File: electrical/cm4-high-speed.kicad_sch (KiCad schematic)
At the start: 1 part

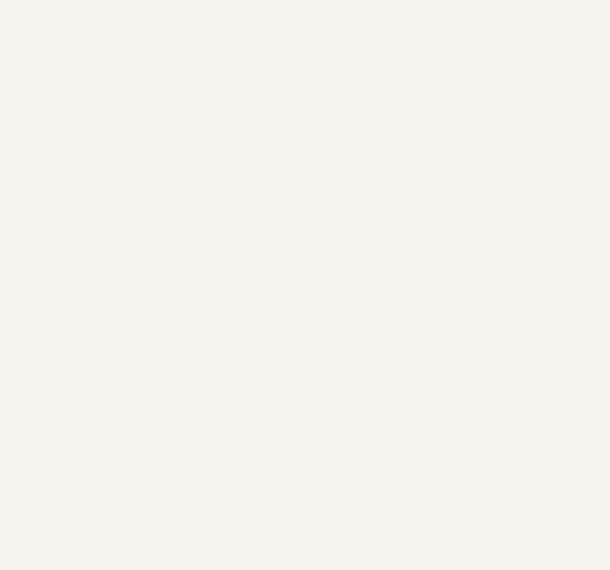
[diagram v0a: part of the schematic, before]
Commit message: Add USB-C and 7-port switch IC libraries
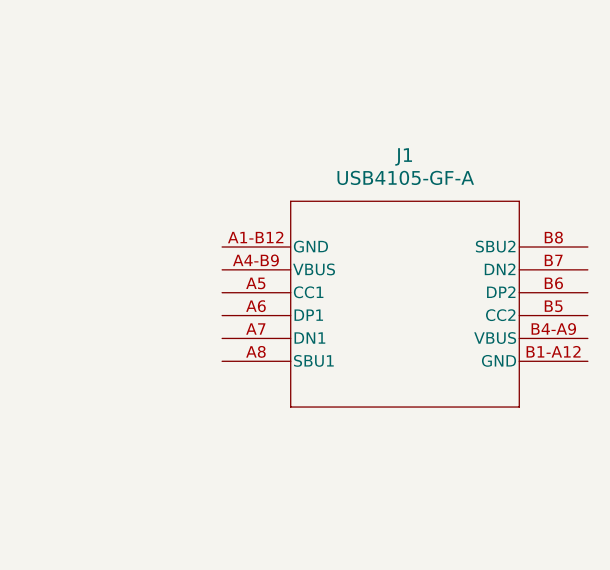
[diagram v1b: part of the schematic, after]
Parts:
- added J1: USB4105-GF-A, USB4105_GCT, symbol USB4105-GF-A:USB4105-GF-A
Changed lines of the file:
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@@
+	)
+	(symbol
+		(lib_id "USB4105-GF-A:USB4105-GF-A")
+		(at 200.66 57.15 0)
+		(unit 1)
+		(exclude_from_sim no)
+		(in_bom yes)
+		(on_board yes)
+		(dnp no)
+		(fields_autoplaced yes)
+		(property "Reference" "J1"
+			(at 220.98 46.99 0)
+			(effects
+				(font
+					(size 1.524 1.524)
+				)
+			)
+		)
+		(property "Value" "USB4105-GF-A"
+			(at 220.98 49.53 0)
+			(effects
+				(font
+					(size 1.524 1.524)
+				)
+			)
+		)
+		(property "Footprint" "USB4105_GCT"
+			(at 200.66 57.15 0)
+			(effects
+				(font
+					(size 1.27 1.27)
+					(italic yes)
+				)
+				(hide yes)
+			)
+		)
+		(property "Datasheet" "USB4105-GF-A"
+			(at 200.66 57.15 0)
+			(effects
+				(font
+					(size 1.27 1.27)
+					(italic yes)
+				)
+				(hide yes)
+			)
+		)
+		(property "Description" ""
+			(at 200.66 57.15 0)
+			(effects
+				(font
+					(size 1.27 1.27)
+				)
+				(hide yes)
+			)
+		)
+		(pin "A6"
+		)
+		(pin "A5"
+		)
+		(pin "B8"
+		)
+		(pin "B5"
+		)
+		(pin "B1-A12"
+		)
+		(pin "B7"
+		)
+		(pin "B4-A9"
+		)
+		(pin "A4-B9"
+		)
+		(pin "A7"
+		)
+		(pin "A1-B12"
+		)
+		(pin "A8"
+		)
+		(pin "B6"
+		)
+		(instances
+			(project ""
+				(path "/87b93ef3-3469-436c-9ae8-16e6c9607244/caa71f4c-454d-4ac9-b287-456eafb34991"
+					(reference "J1")
+					(unit 1)
+				)
+			)
+		)
 	)
 	(symbol

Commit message: RJ-45 <-> KSZ9897R schematic connections
Also switched to a different RJ-45 port: Belfuse 0826-1G1T-23-F
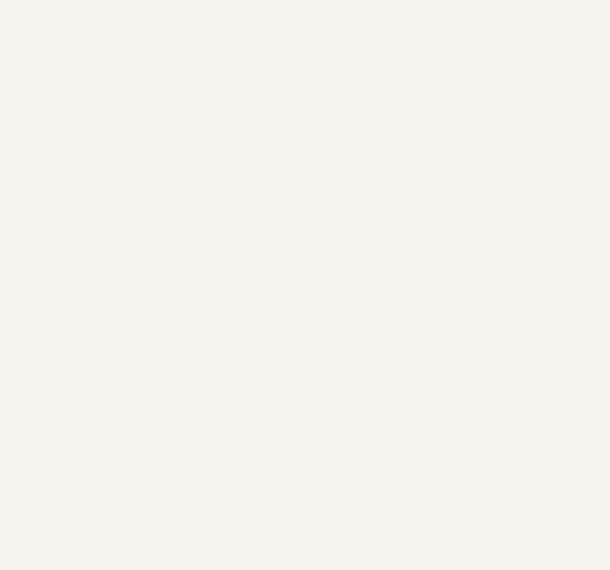
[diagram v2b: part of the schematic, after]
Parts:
- removed J1: USB4105-GF-A, USB4105_GCT, symbol USB4105-GF-A:USB4105-GF-A
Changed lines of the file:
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@@
-	)
-	(symbol
-		(lib_id "USB4105-GF-A:USB4105-GF-A")
-		(at 200.66 57.15 0)
-		(unit 1)
-		(exclude_from_sim no)
-		(in_bom yes)
-		(on_board yes)
-		(dnp no)
-		(fields_autoplaced yes)
-		(property "Reference" "J1"
-			(at 220.98 46.99 0)
-			(effects
-				(font
-					(size 1.524 1.524)
-				)
-			)
-		)
-		(property "Value" "USB4105-GF-A"
-			(at 220.98 49.53 0)
-			(effects
-				(font
-					(size 1.524 1.524)
-				)
-			)
-		)
-		(property "Footprint" "USB4105_GCT"
-			(at 200.66 57.15 0)
-			(effects
-				(font
-					(size 1.27 1.27)
-					(italic yes)
-				)
-				(hide yes)
-			)
-		)
-		(property "Datasheet" "USB4105-GF-A"
-			(at 200.66 57.15 0)
-			(effects
-				(font
-					(size 1.27 1.27)
-					(italic yes)
-				)
-				(hide yes)
-			)
-		)
-		(property "Description" ""
-			(at 200.66 57.15 0)
-			(effects
-				(font
-					(size 1.27 1.27)
-				)
-				(hide yes)
-			)
-		)
-		(pin "A6"
-		)
-		(pin "A5"
-		)
-		(pin "B8"
-		)
-		(pin "B5"
-		)
-		(pin "B1-A12"
-		)
-		(pin "B7"
-		)
-		(pin "B4-A9"
-		)
-		(pin "A4-B9"
-		)
-		(pin "A7"
-		)
-		(pin "A1-B12"
-		)
-		(pin "A8"
-		)
-		(pin "B6"
-		)
-		(instances
-			(project ""
-				(path "/87b93ef3-3469-436c-9ae8-16e6c9607244/caa71f4c-454d-4ac9-b287-456eafb34991"
-					(reference "J1")
-					(unit 1)
-				)
-			)
-		)
 	)
 	(symbol
